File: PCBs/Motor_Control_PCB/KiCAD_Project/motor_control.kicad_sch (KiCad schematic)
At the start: 19 parts, among them J1 NP_Conn_01x06, U1 1-0000452, U2 1-0001532

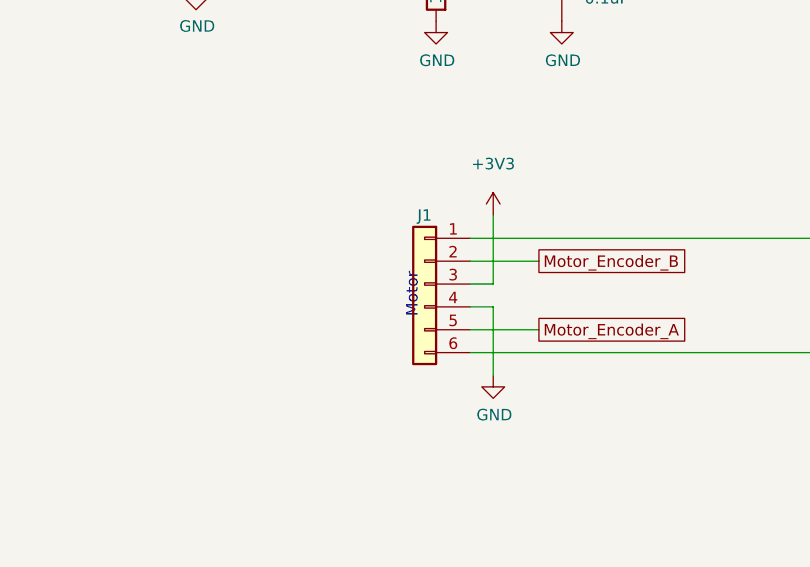
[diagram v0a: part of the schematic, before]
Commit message: Digital PCB Revisions: Fixed ERC Footprint/Symbol Errors Fixed Remaining ERC Errors Relocated U7 to bottom of PCB
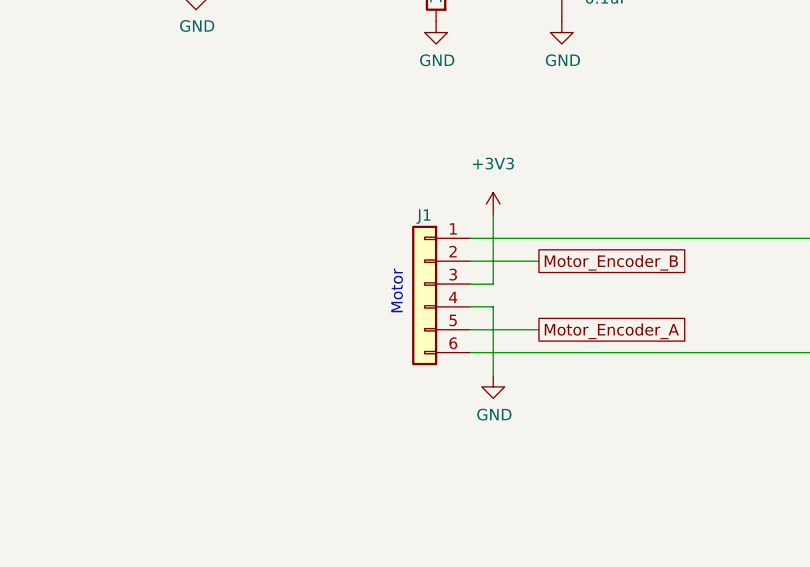
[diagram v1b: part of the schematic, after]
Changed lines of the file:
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@@
 	(text "Motor"
 		(exclude_from_sim no)
-		(at 94.615 101.6 90)
+		(at 92.964 101.346 90)
 		(effects
 			(font

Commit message: Fixed Motor PCB ERC Issues and Copper to Edge Clearence
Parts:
- H1, H2, H3, H4: now left out of the parts list
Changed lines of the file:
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@@
 		(unit 1)
 		(exclude_from_sim no)
-		(in_bom yes)
+		(in_bom no)
 		(on_board yes)
 		(dnp no)
@@
 		(unit 1)
 		(exclude_from_sim no)
-		(in_bom yes)
+		(in_bom no)
 		(on_board yes)
 		(dnp no)
@@
 		(unit 1)
 		(exclude_from_sim no)
-		(in_bom yes)
+		(in_bom no)
 		(on_board yes)
 		(dnp no)
@@
 		(unit 1)
 		(exclude_from_sim no)
-		(in_bom yes)
-		(on_board yes)
-		(dnp no)
+		(in_bom no)
+		(on_board yes)
+		(dnp no)
